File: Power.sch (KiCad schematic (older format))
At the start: 0 parts

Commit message: M3 U5
Power protection and filtering
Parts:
- added C? (x2): C, ~, symbol C
- added F? (x4): FUSE, ~, symbol FUSE
- added L? (x2): INDUCTOR, ~, symbol INDUCTOR
- added P?: CONN_12X2, symbol CONN_12X2
- added R?: R, ~, symbol R
- added SW?: SWITCH_INV, ~, symbol SWITCH_INV
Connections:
- new net: F?.1, P?.10 (P10)
- new net: F?.1, P?.14 (P14)
- new net: P?.16 (P16), SW?.2
- new net: F?.1, P?.2 (P2)
- new net: F?.1, P?.4 (P4), P?.6 (P6)
- new net: R?.1, SW?.1
- new net +12P: C?.1, F?.2, L?.1, L?.2
- new net +3.3V: F?.2, R?.2
- new net +5V: F?.2
- new net -12P: C?.2, F?.2, L?.1
- new net GND: C?.1, C?.2, P?.3 (P3), P?.5 (P5), SW?.3
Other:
- note added: "I think 1 and 2 should be hooked up together"

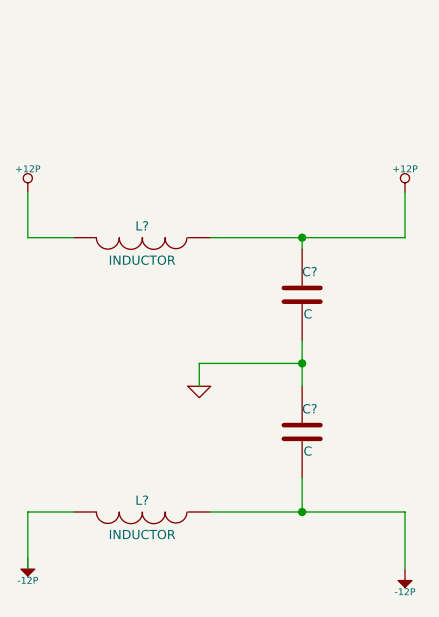
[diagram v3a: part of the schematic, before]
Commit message: M3 U6
Power Control, Conditioning and Monitoring module
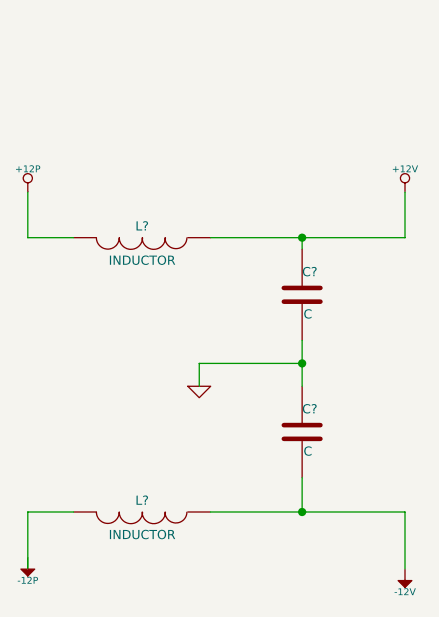
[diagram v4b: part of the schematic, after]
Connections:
- net +12P: no longer C?.1, L?.1
- net -12P: no longer C?.2, L?.1
- new net +12V: C?.1, L?.1
- new net -12V: C?.2, L?.1
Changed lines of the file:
@@
 Sheet 5 9
 Title ""
-Date "12 feb 2014"
+Date "14 feb 2014"
 Rev ""
 Comp ""
@@
 	1    0    0    -1
 $EndComp
+Text Notes 1850 1300 0    60   ~ 0
+I think 1 and 2 should be hooked up together
 Wire Wire Line
 	1550 1600 2250 1600
@@
 Connection ~ 9850 3250
 $Comp
-L +12P #PWR?
-U 1 1 52FB2674
+L +12V #PWR?
+U 1 1 52FD9E6A
 P 10300 1850
-F 0 "#PWR?" H 10300 1820 30  0001 C CNN
-F 1 "+12P" H 10300 1950 30  0000 C CNN
+F 0 "#PWR?" H 10300 1800 20  0001 C CNN
+F 1 "+12V" H 10300 1950 30  0000 C CNN
 F 2 "" H 10300 1850 60  0000 C CNN
 F 3 "" H 10300 1850 60  0000 C CNN
@@
 $EndComp
 $Comp
-L -12P #PWR?
-U 1 1 52FB2683
+L -12V #PWR?
+U 1 1 52FD9E79
 P 10300 3500
 F 0 "#PWR?" H 10300 3630 20  0001 C CNN
-F 1 "-12P" H 10300 3600 30  0000 C CNN
+F 1 "-12V" H 10300 3600 30  0000 C CNN
 F 2 "" H 10300 3500 60  0000 C CNN
 F 3 "" H 10300 3500 60  0000 C CNN
@@
 	-1   0    0    1
 $EndComp
-Text Notes 1850 1300 0    60   ~ 0
-I think 1 and 2 should be hooked up together
 $EndSCHEMATC

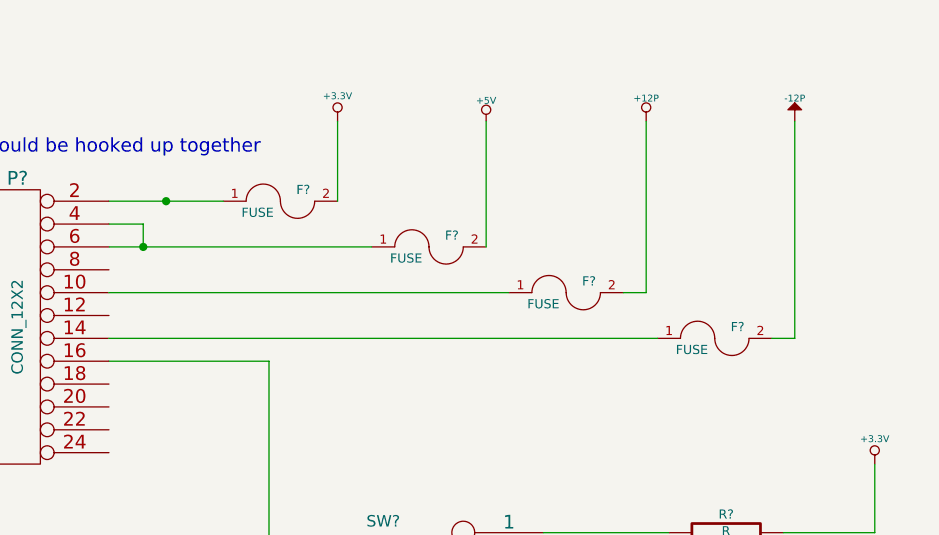
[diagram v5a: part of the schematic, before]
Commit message: M3 U9
Revisiting the Current/Fan Module
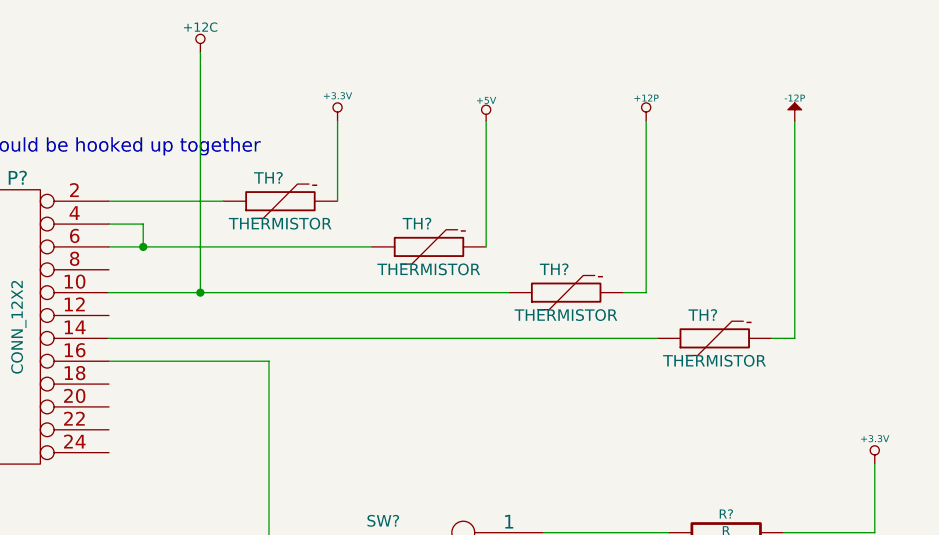
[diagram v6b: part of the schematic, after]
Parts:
- removed F? (x4): FUSE, ~, symbol FUSE
- added TH? (x4): THERMISTOR, ~, symbol THERMISTOR
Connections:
- net +12P: now also TH?.2
- net +3.3V: now also TH?.2
- net +5V: now also TH?.2
- net -12P: now also TH?.2
- net +12C: now reaches P?.10 (P10)
- net +12C: now also TH?.1
- net at P?.14 (P14): now also TH?.1
- net at P?.2 (P2): now also TH?.1
- net at P?.4 (P4), P?.6 (P6): now also TH?.1
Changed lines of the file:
@@
-$EndComp
-$Comp
-L FUSE F?
-U 1 1 52FB0285
-P 3800 1500
-F 0 "F?" H 3900 1550 40  0000 C CNN
-F 1 "FUSE" H 3700 1450 40  0000 C CNN
-F 2 "~" H 3800 1500 60  0000 C CNN
-F 3 "~" H 3800 1500 60  0000 C CNN
-	1    3800 1500
-	1    0    0    -1
-$EndComp
-$Comp
-L FUSE F?
-U 1 1 52FB0292
-P 4450 1700
-F 0 "F?" H 4550 1750 40  0000 C CNN
-F 1 "FUSE" H 4350 1650 40  0000 C CNN
-F 2 "~" H 4450 1700 60  0000 C CNN
-F 3 "~" H 4450 1700 60  0000 C CNN
-	1    4450 1700
-	1    0    0    -1
-$EndComp
-$Comp
-L FUSE F?
-U 1 1 52FB0298
-P 5050 1900
-F 0 "F?" H 5150 1950 40  0000 C CNN
-F 1 "FUSE" H 4950 1850 40  0000 C CNN
-F 2 "~" H 5050 1900 60  0000 C CNN
-F 3 "~" H 5050 1900 60  0000 C CNN
-	1    5050 1900
-	1    0    0    -1
-$EndComp
-$Comp
-L FUSE F?
-U 1 1 52FB029E
-P 5700 2100
-F 0 "F?" H 5800 2150 40  0000 C CNN
-F 1 "FUSE" H 5600 2050 40  0000 C CNN
-F 2 "~" H 5700 2100 60  0000 C CNN
-F 3 "~" H 5700 2100 60  0000 C CNN
-	1    5700 2100
-	1    0    0    -1
 $EndComp
 $Comp
@@
 Wire Wire Line
 	3050 1500 3550 1500
-Connection ~ 3300 1500
 Wire Wire Line
 	3050 1600 3200 1600
@@
 	-1   0    0    1
 $EndComp
+Wire Wire Line
+	3450 850  3450 1900
+Connection ~ 3450 1900
+$Comp
+L +12C #PWR?
+U 1 1 5300F6E3
+P 3450 850
+F 0 "#PWR?" H 3450 820 30  0001 C CNN
+F 1 "+12C" H 3450 960 40  0000 C CNN
+F 2 "" H 3450 850 60  0000 C CNN
+F 3 "" H 3450 850 60  0000 C CNN
+	1    3450 850
+	1    0    0    -1
+$EndComp
+$Comp
+L THERMISTOR TH?
+U 1 1 53011495
+P 5700 2100
+F 0 "TH?" V 5800 2150 50  0000 C CNN
+F 1 "THERMISTOR" V 5600 2100 50  0000 C CNN
+F 2 "~" H 5700 2100 60  0000 C CNN
+F 3 "~" H 5700 2100 60  0000 C CNN
+	1    5700 2100
+	0    -1   -1   0
+$EndComp
+$Comp
+L THERMISTOR TH?
+U 1 1 530114A2
+P 5050 1900
+F 0 "TH?" V 5150 1950 50  0000 C CNN
+F 1 "THERMISTOR" V 4950 1900 50  0000 C CNN
+F 2 "~" H 5050 1900 60  0000 C CNN
+F 3 "~" H 5050 1900 60  0000 C CNN
+	1    5050 1900
+	0    -1   -1   0
+$EndComp
+$Comp
+L THERMISTOR TH?
+U 1 1 530114A8
+P 4450 1700
+F 0 "TH?" V 4550 1750 50  0000 C CNN
+F 1 "THERMISTOR" V 4350 1700 50  0000 C CNN
+F 2 "~" H 4450 1700 60  0000 C CNN
+F 3 "~" H 4450 1700 60  0000 C CNN
+	1    4450 1700
+	0    -1   -1   0
+$EndComp
+$Comp
+L THERMISTOR TH?
+U 1 1 530114AE
+P 3800 1500
+F 0 "TH?" V 3900 1550 50  0000 C CNN
+F 1 "THERMISTOR" V 3700 1500 50  0000 C CNN
+F 2 "~" H 3800 1500 60  0000 C CNN
+F 3 "~" H 3800 1500 60  0000 C CNN
+	1    3800 1500
+	0    -1   -1   0
+$EndComp
 $EndSCHEMATC
